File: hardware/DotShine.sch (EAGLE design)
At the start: 54 parts, among them CN1 1X4-BIG, IC1 CAT24M010TS, IC3 SI1145, J3 USB-MICROB, U1 ATMEGA328P-MU-QFN32, U2 TMP102, U3 ATSHA204-TSU, X2 MC-RTC-RV-4162-C7-I2C, X3 S4B-ZR

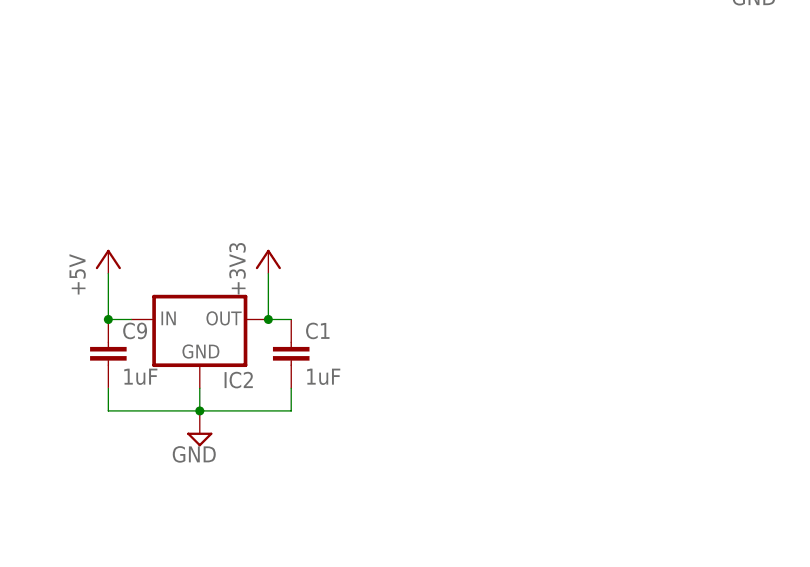
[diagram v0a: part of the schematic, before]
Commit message: Add schottky@LDO for solar powered operation
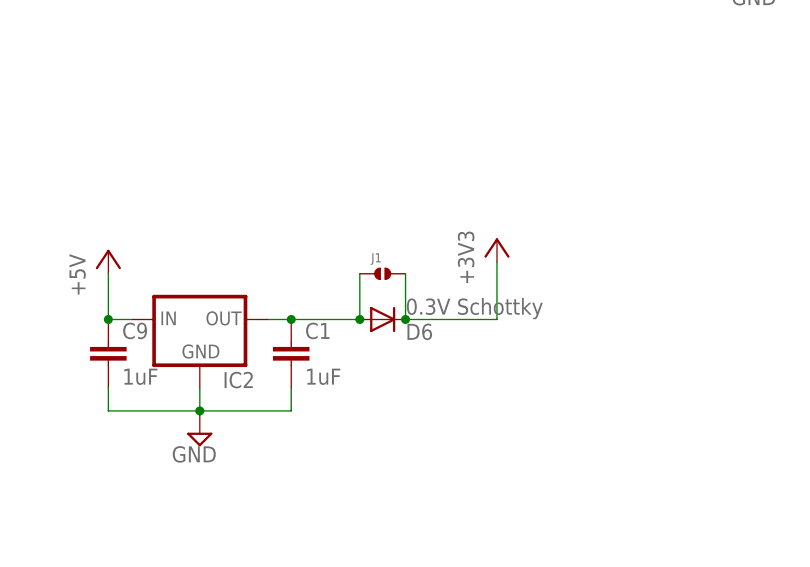
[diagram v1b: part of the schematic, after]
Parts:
- added D6: 0.3V Schottky, diode:DIODE-SOD523
- added J1: (no value), solderjumper:SOLDERJUMPER.2.MED
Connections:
- new net N$25: C1.1, D6.A, IC2.OUT, J1.1
- net +3V3: now also D6.C, J1.2; no longer C1.1, IC2.OUT
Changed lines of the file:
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@@
 <part name="C7" library="adafruit" deviceset="CPOL-US" device="CT7343" value="1500uF 4V"/>
 <part name="+3V3" library="supply1" deviceset="+3V3" device=""/>
+<part name="D6" library="diode" deviceset="DIODE-" device="SOD523" value="0.3V Schottky"/>
+<part name="J1" library="solderjumper" deviceset="SOLDERJUMPER.2" device=".MED"/>
 </parts>
 <sheets>
@@
 <instance part="SUPPLY12" gate="GND" x="160.02" y="152.4" rot="R90"/>
 <instance part="SUPPLY27" gate="GND" x="144.78" y="-48.26" rot="MR0"/>
-<instance part="+3V19" gate="G$1" x="152.4" y="-27.94"/>
+<instance part="+3V19" gate="G$1" x="177.8" y="-26.67"/>
 <instance part="P+4" gate="1" x="134.62" y="-27.94"/>
 <instance part="C1" gate="G$1" x="154.94" y="-38.1"/>
@@
 <instance part="C7" gate="G$1" x="67.31" y="-222.25" rot="MR0"/>
 <instance part="+3V3" gate="G$1" x="31.75" y="-199.39"/>
+<instance part="D6" gate="G$1" x="165.1" y="-35.56" rot="MR180"/>
+<instance part="J1" gate="G$1" x="165.1" y="-30.48"/>
 </instances>
 <busses>
@@
 <wire x1="76.2" y1="-77.47" x2="68.58" y2="-77.47" width="0.1524" layer="91"/>
 <pinref part="+3V7" gate="G$1" pin="+3V3"/>
-</segment>
-<segment>
-<pinref part="+3V19" gate="G$1" pin="+3V3"/>
-<wire x1="152.4" y1="-30.48" x2="152.4" y2="-35.56" width="0.1524" layer="91"/>
-<pinref part="C1" gate="G$1" pin="1"/>
-<wire x1="154.94" y1="-35.56" x2="152.4" y2="-35.56" width="0.1524" layer="91"/>
-<pinref part="IC2" gate="G$1" pin="OUT"/>
-<junction x="152.4" y="-35.56"/>
 </segment>
 <segment>
@@
 <junction x="31.75" y="-209.55"/>
 </segment>
+<segment>
+<pinref part="J1" gate="G$1" pin="2"/>
+<pinref part="D6" gate="G$1" pin="C"/>
+<wire x1="167.64" y1="-30.48" x2="167.64" y2="-35.56" width="0.1524" layer="91"/>
+<junction x="167.64" y="-35.56"/>
+<pinref part="+3V19" gate="G$1" pin="+3V3"/>
+<wire x1="167.64" y1="-35.56" x2="177.8" y2="-35.56" width="0.1524" layer="91"/>
+<wire x1="177.8" y1="-35.56" x2="177.8" y2="-29.21" width="0.1524" layer="91"/>
+</segment>
 </net>
 <net name="ADCENA" class="0">
@@
 </segment>
 </net>
+<net name="N$25" class="0">
+<segment>
+<pinref part="C1" gate="G$1" pin="1"/>
+<pinref part="IC2" gate="G$1" pin="OUT"/>
+<wire x1="154.94" y1="-35.56" x2="152.4" y2="-35.56" width="0.1524" layer="91"/>
+<pinref part="D6" gate="G$1" pin="A"/>
+<wire x1="162.56" y1="-35.56" x2="154.94" y2="-35.56" width="0.1524" layer="91"/>
+<junction x="154.94" y="-35.56"/>
+<pinref part="J1" gate="G$1" pin="1"/>
+<wire x1="162.56" y1="-30.48" x2="162.56" y2="-35.56" width="0.1524" layer="91"/>
+<junction x="162.56" y="-35.56"/>
+</segment>
+</net>

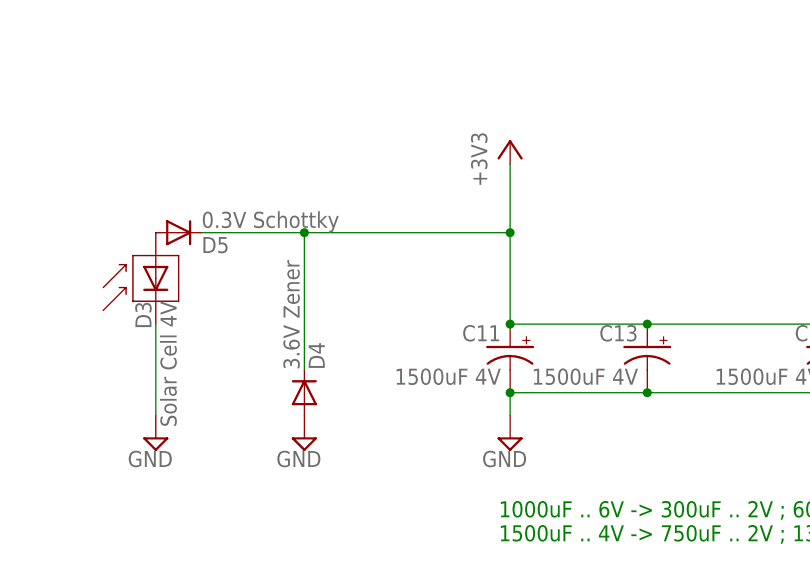
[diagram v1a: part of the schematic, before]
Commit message: Add second zener if using large solar panel
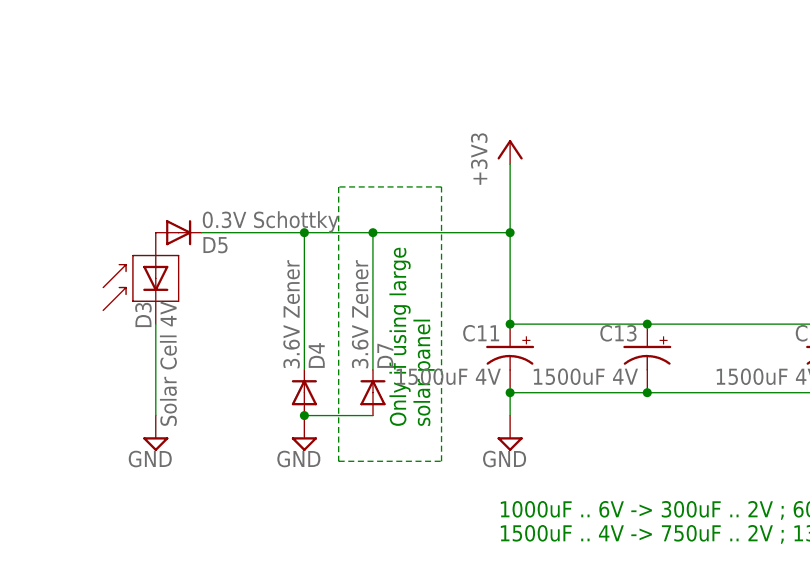
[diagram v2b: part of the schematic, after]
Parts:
- added D7: 3.6V Zener, diode:DIODE-SOD523
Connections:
- net +3V3: now also D7.C
- net GND: now also D7.A
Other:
- note added: "Only if using large solar panel"
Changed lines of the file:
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@@
 <part name="D6" library="diode" deviceset="DIODE-" device="SOD523" value="0.3V Schottky"/>
 <part name="J1" library="solderjumper" deviceset="SOLDERJUMPER.2" device=".MED"/>
+<part name="D7" library="diode" deviceset="DIODE-" device="SOD523" value="3.6V Zener"/>
 </parts>
 <sheets>
@@
 <text x="30.48" y="-243.84" size="1.778" layer="91">1000uF .. 6V -&gt; 300uF .. 2V ; 600 .. 3.6V -&gt; buget: 600-300 = 300uF
 1500uF .. 4V -&gt; 750uF .. 2V ; 1350.. 3.6V-&gt; buget: 1350-750 = 600uF</text>
+<text x="22.86" y="-231.14" size="1.778" layer="91" rot="R90">Only if using large
+solar panel</text>
 </plain>
 <instances>
@@
 <instance part="D6" gate="G$1" x="165.1" y="-35.56" rot="MR180"/>
 <instance part="J1" gate="G$1" x="165.1" y="-30.48"/>
+<instance part="D7" gate="G$1" x="16.51" y="-227.33" rot="MR90"/>
 </instances>
 <busses>
@@
 <pinref part="D4" gate="G$1" pin="A"/>
 <pinref part="SUPPLY34" gate="GND" pin="GND"/>
+<pinref part="D7" gate="G$1" pin="A"/>
+<wire x1="16.51" y1="-229.87" x2="8.89" y2="-229.87" width="0.1524" layer="91"/>
+<junction x="8.89" y="-229.87"/>
 </segment>
 <segment>
@@
 <pinref part="D5" gate="G$1" pin="C"/>
 <wire x1="-2.54" y1="-209.55" x2="8.89" y2="-209.55" width="0.1524" layer="91"/>
-<wire x1="8.89" y1="-209.55" x2="31.75" y2="-209.55" width="0.1524" layer="91"/>
+<wire x1="8.89" y1="-209.55" x2="16.51" y2="-209.55" width="0.1524" layer="91"/>
 <pinref part="D4" gate="G$1" pin="C"/>
+<wire x1="16.51" y1="-209.55" x2="31.75" y2="-209.55" width="0.1524" layer="91"/>
 <wire x1="8.89" y1="-224.79" x2="8.89" y2="-209.55" width="0.1524" layer="91"/>
 <junction x="8.89" y="-209.55"/>
@@
 <wire x1="31.75" y1="-201.93" x2="31.75" y2="-209.55" width="0.1524" layer="91"/>
 <junction x="31.75" y="-209.55"/>
+<pinref part="D7" gate="G$1" pin="C"/>
+<wire x1="16.51" y1="-224.79" x2="16.51" y2="-209.55" width="0.1524" layer="91"/>
+<junction x="16.51" y="-209.55"/>
 </segment>
 <segment>
@@
 </segment>
 </net>
+<net name="N$33" class="0">
+<segment>
+<wire x1="12.7" y1="-204.47" x2="12.7" y2="-234.95" width="0.1524" layer="91" style="shortdash"/>
+<wire x1="12.7" y1="-234.95" x2="24.13" y2="-234.95" width="0.1524" layer="91" style="shortdash"/>
+<wire x1="24.13" y1="-234.95" x2="24.13" y2="-204.47" width="0.1524" layer="91" style="shortdash"/>
+<wire x1="24.13" y1="-204.47" x2="12.7" y2="-204.47" width="0.1524" layer="91" style="shortdash"/>
+</segment>
+</net>

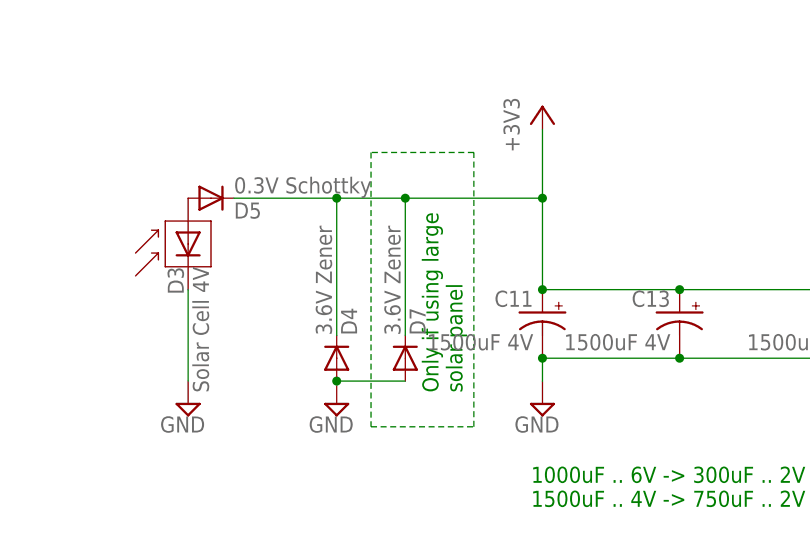
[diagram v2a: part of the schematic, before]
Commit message: Add second strong zener if using large solar panel
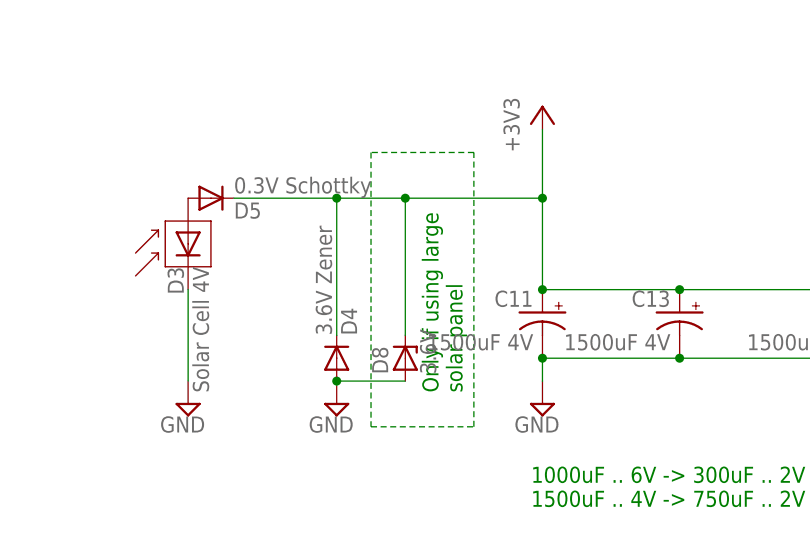
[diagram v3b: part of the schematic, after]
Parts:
- removed D7: 3.6V Zener, diode:DIODE-SOD523
- added D8: 3.6V, diode:ZENER-DIODESOD80C
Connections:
- net +3V3: now also D8.C; no longer D7.C
- net GND: now also D8.A; no longer D7.A

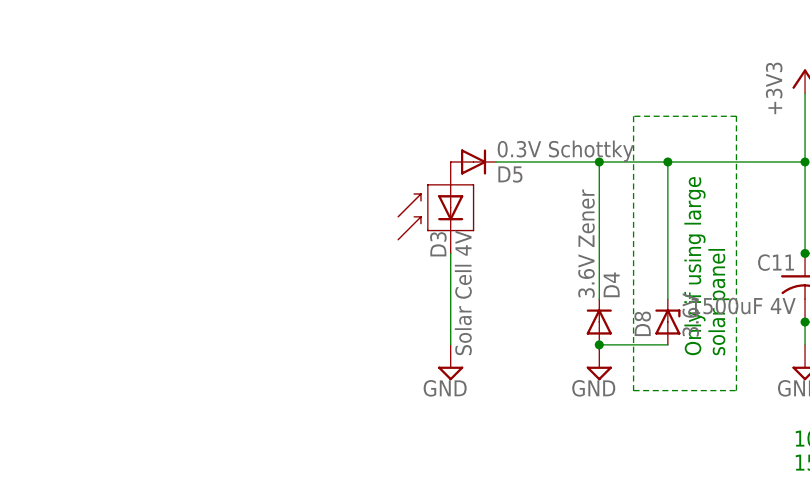
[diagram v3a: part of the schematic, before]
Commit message: Connect + of solar together, share Schottky
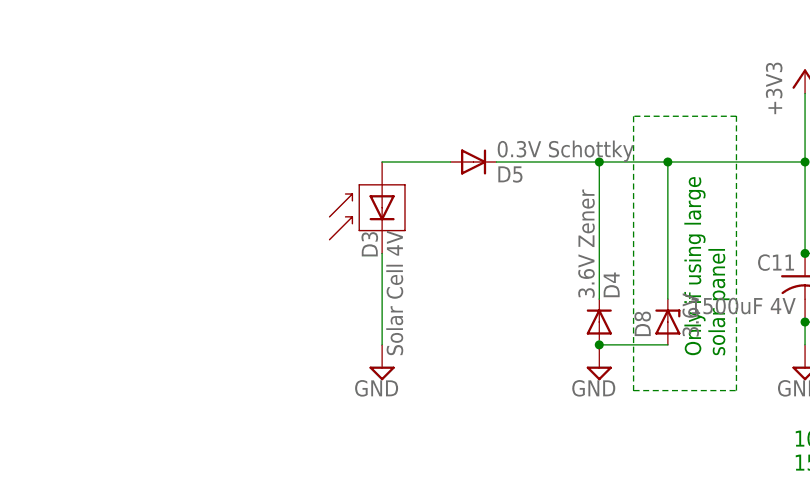
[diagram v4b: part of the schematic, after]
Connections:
- net N$5 renamed SOLAR_OUT
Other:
- moved on the sheet: D3
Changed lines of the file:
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@@
 <setting verticaltext="up"/>
 </settings>
-<grid distance="0.05" unitdist="inch" unit="inch" style="lines" multiple="1" display="no" altdistance="0.01" altunitdist="inch" altunit="inch"/>
+<grid distance="0.1" unitdist="inch" unit="inch" style="lines" multiple="1" display="no" altdistance="0.01" altunitdist="inch" altunit="inch"/>
 <layers>
 <layer number="1" name="Top" color="4" fill="1" visible="no" active="no"/>
@@
 <instance part="SUPPLY32" gate="GND" x="57.15" y="2.54" rot="R180"/>
 <instance part="U$3" gate="G$1" x="57.15" y="-5.08" rot="R90"/>
-<instance part="D3" gate="G$1" x="-7.62" y="-214.63" rot="MR270"/>
+<instance part="D3" gate="G$1" x="-15.24" y="-214.63" rot="MR270"/>
 <instance part="D4" gate="G$1" x="8.89" y="-227.33" rot="MR90"/>
-<instance part="SUPPLY33" gate="GND" x="-7.62" y="-232.41" rot="MR0"/>
+<instance part="SUPPLY33" gate="GND" x="-15.24" y="-232.41" rot="MR0"/>
 <instance part="C11" gate="G$1" x="31.75" y="-222.25" rot="MR0"/>
 <instance part="SUPPLY35" gate="GND" x="31.75" y="-232.41" rot="MR0"/>
@@
 <pinref part="D3" gate="G$1" pin="C"/>
 <pinref part="SUPPLY33" gate="GND" pin="GND"/>
-<wire x1="-7.62" y1="-219.71" x2="-7.62" y2="-229.87" width="0.1524" layer="91"/>
+<wire x1="-15.24" y1="-219.71" x2="-15.24" y2="-229.87" width="0.1524" layer="91"/>
 </segment>
 <segment>
@@
 </segment>
 </net>
-<net name="N$5" class="0">
+<net name="SOLAR_OUT" class="0">
 <segment>
 <pinref part="D3" gate="G$1" pin="A"/>
 <pinref part="D5" gate="G$1" pin="A"/>
-</segment>
-</net>
+<wire x1="-15.24" y1="-209.55" x2="-7.62" y2="-209.55" width="0.1524" layer="91"/>
+</segment>
+</net>

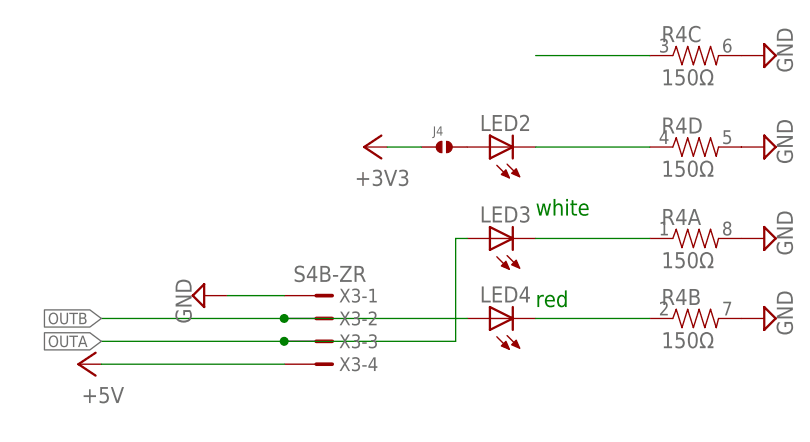
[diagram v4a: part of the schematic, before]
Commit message: On Led -> USB, now at 5V. Only on when usb present
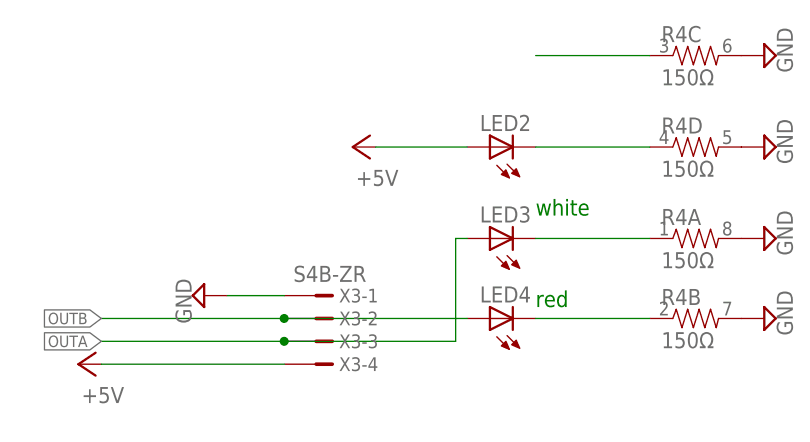
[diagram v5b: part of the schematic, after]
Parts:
- removed J4: (no value), solderjumper:SOLDERJUMPER.2.MED
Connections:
- removed net N$12: J4.2, LED2.A
- net +3V3: no longer J4.1
- net +5V: now also LED2.A
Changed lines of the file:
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@@
 <setting verticaltext="up"/>
 </settings>
-<grid distance="0.1" unitdist="inch" unit="inch" style="lines" multiple="1" display="no" altdistance="0.01" altunitdist="inch" altunit="inch"/>
+<grid distance="0.05" unitdist="inch" unit="inch" style="lines" multiple="1" display="no" altdistance="0.01" altunitdist="inch" altunit="inch"/>
 <layers>
 <layer number="1" name="Top" color="4" fill="1" visible="no" active="no"/>
@@
 <part name="LOGO1" library="Spark" deviceset="OSHW-LOGO" device="S"/>
 <part name="SUPPLY29" library="supply2" deviceset="GND" device=""/>
-<part name="+3V1" library="supply1" deviceset="+3V3" device=""/>
 <part name="R7" library="SparkFun" deviceset="RESISTOR-ARRAY" device="0603-ARV" value="4.7kΩ"/>
 <part name="+3V8" library="supply1" deviceset="+3V3" device=""/>
@@
 <part name="IC2" library="MCP1700" deviceset="MCP1700" device="TT"/>
 <part name="C9" library="rcl" deviceset="C-EU" device="C0603" value="1uF"/>
-<part name="J4" library="solderjumper" deviceset="SOLDERJUMPER.2" device=".MED"/>
 <part name="LED5" library="SparkFun" deviceset="LED" device="0603"/>
 <part name="SUPPLY28" library="supply2" deviceset="GND" device=""/>
@@
 <part name="J1" library="solderjumper" deviceset="SOLDERJUMPER.2" device=".MED"/>
 <part name="D8" library="diode" deviceset="ZENER-DIODE" device="SOD80C" value="3.6V"/>
+<part name="P+1" library="supply1" deviceset="+5V" device=""/>
 </parts>
 <sheets>
@@
 <instance part="LOGO1" gate="G$1" x="-22.86" y="104.14"/>
 <instance part="SUPPLY29" gate="GND" x="160.02" y="142.24" rot="R90"/>
-<instance part="+3V1" gate="G$1" x="115.57" y="142.24" rot="R90"/>
 <instance part="R7" gate="A" x="78.74" y="-10.16"/>
 <instance part="R7" gate="B" x="78.74" y="-15.24"/>
@@
 <instance part="IC2" gate="G$1" x="144.78" y="-35.56"/>
 <instance part="C9" gate="G$1" x="134.62" y="-38.1"/>
-<instance part="J4" gate="G$1" x="124.46" y="142.24"/>
 <instance part="LED5" gate="G$1" x="-45.72" y="53.34"/>
 <instance part="SUPPLY28" gate="GND" x="-45.72" y="45.72" rot="MR0"/>
@@
 <instance part="J1" gate="G$1" x="165.1" y="-30.48"/>
 <instance part="D8" gate="G$1" x="16.51" y="-227.33" rot="R90"/>
+<instance part="P+1" gate="1" x="114.3" y="142.24" rot="R90"/>
 </instances>
 <busses>
@@
 <wire x1="53.34" y1="-119.38" x2="73.66" y2="-119.38" width="0.1524" layer="91"/>
 <wire x1="73.66" y1="-119.38" x2="73.66" y2="-116.84" width="0.1524" layer="91"/>
-</segment>
-<segment>
-<pinref part="J4" gate="G$1" pin="1"/>
-<pinref part="+3V1" gate="G$1" pin="+3V3"/>
-<wire x1="121.92" y1="142.24" x2="118.11" y2="142.24" width="0.1524" layer="91"/>
 </segment>
 <segment>
@@
 <junction x="134.62" y="-35.56"/>
 </segment>
+<segment>
+<pinref part="P+1" gate="1" pin="+5V"/>
+<pinref part="LED2" gate="G$1" pin="A"/>
+<wire x1="127" y1="142.24" x2="116.84" y2="142.24" width="0.1524" layer="91"/>
+</segment>
 </net>
 <net name="N$7" class="0">
@@
 </segment>
 </net>
-<net name="N$12" class="0">
-<segment>
-<pinref part="LED2" gate="G$1" pin="A"/>
-<pinref part="J4" gate="G$1" pin="2"/>
-</segment>
-</net>
